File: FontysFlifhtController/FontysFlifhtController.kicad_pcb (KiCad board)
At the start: 2 copper layers, 44 x 66 mm, 25 parts, among them J1 I2C 1, J10 Motor Control 3, J11 Motor Control 4, J12 Ultrasonic Sensor, J13 Battery Power, J14 RaspberryPi, J2 I2C 2, J3 SPI 1, J4 SPI 2, J6 Camera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

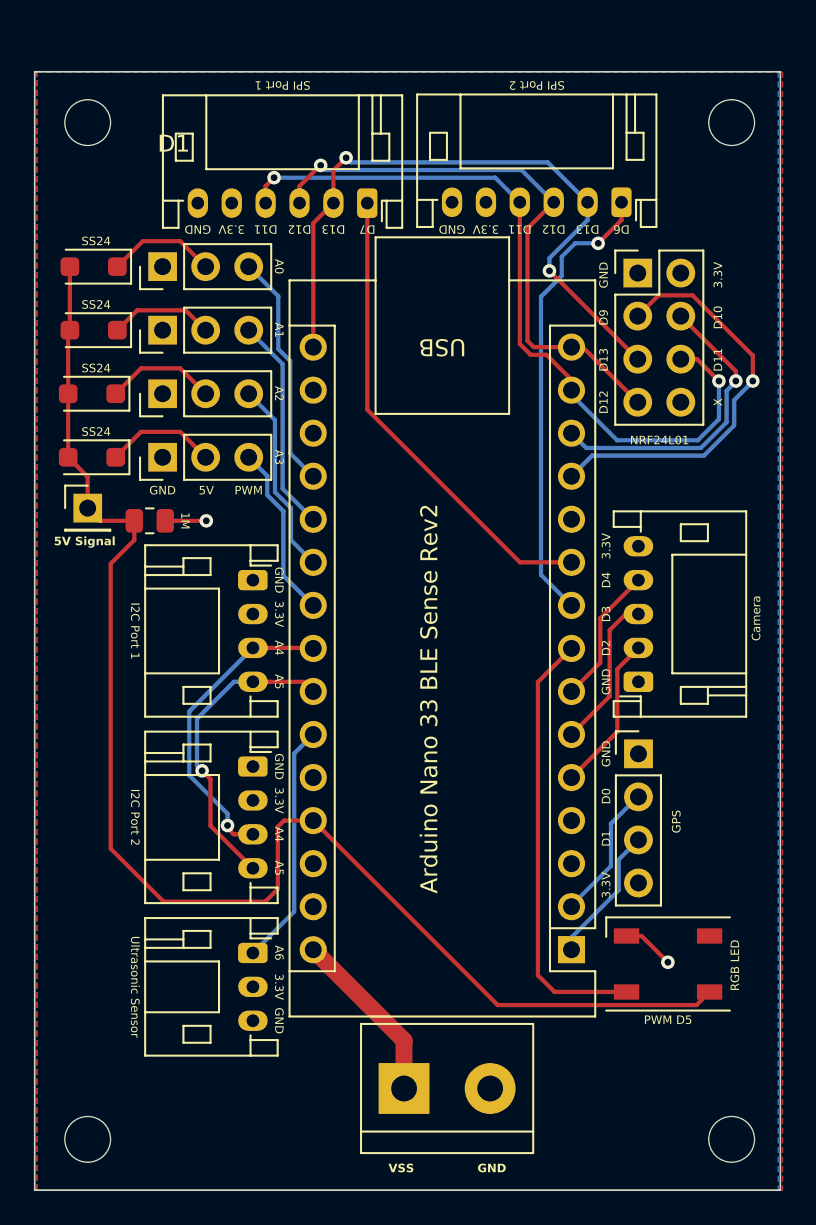
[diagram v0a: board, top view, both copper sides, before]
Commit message: Add turn on/off functionality for the motors
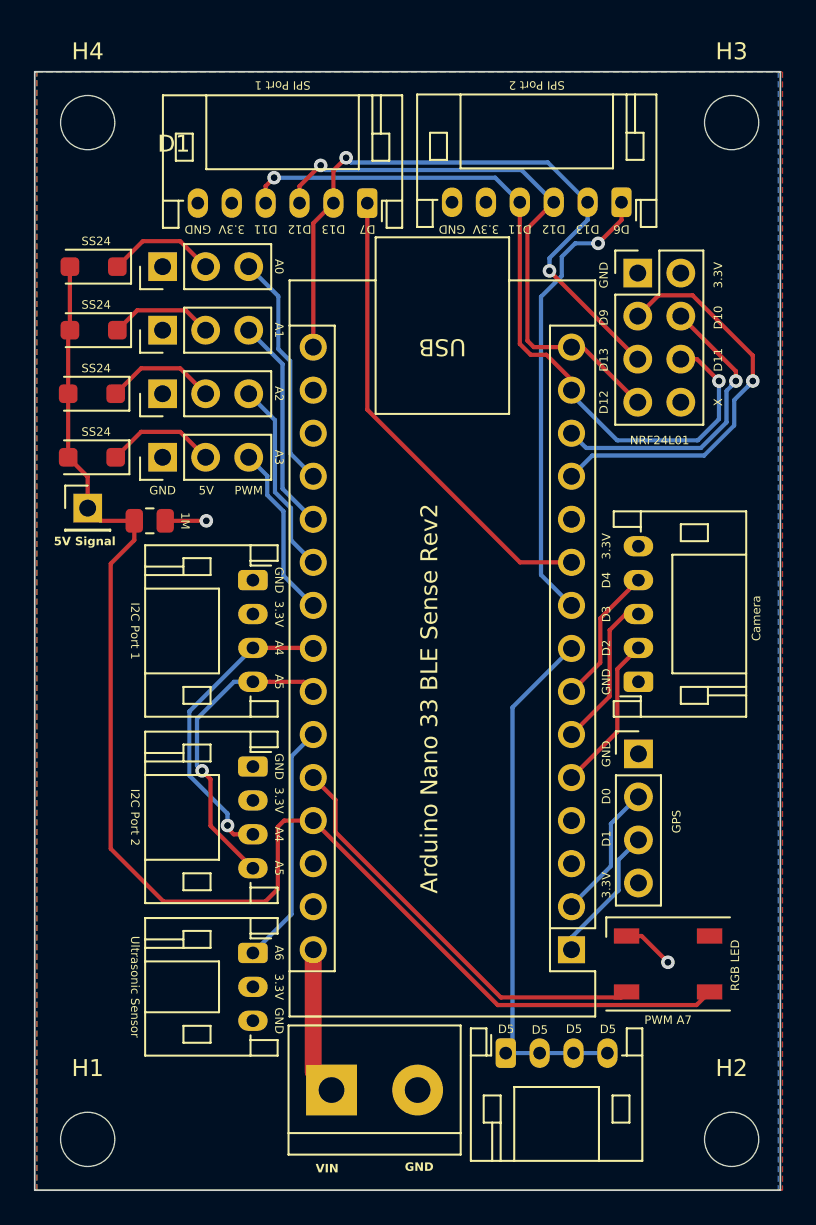
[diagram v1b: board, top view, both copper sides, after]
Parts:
- added J5: Motors On/Off, Connector_JST:JST_PH_S4B-PH-K_1x04_P2.00mm_Horizontal, F.Cu at (136.2, 127.9)
- H1, H2, H3, H4: footprint MountingHole:MountingHole_2.7mm_M2.5 -> MountingHole:MountingHole_3.2mm_M3
- moved J13 4.28 mm to (125.9, 130.1)
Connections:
- A1 pad 26: unconnected-(A1-A7-Pad26) -> /A7
- D2 pad 4: /D5 -> /A7
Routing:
- net /A7: track 0.00 -> 25.1 mm
- net /D5: track 25.7 -> 31.5 mm
- net /VIN: track 10.4 -> 8.73 mm
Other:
- board text added: "D5"
- board text added: "PWM A7"
- board text added: "VIN"
- board text removed: "PWM D5"
- board text removed: "VSS"

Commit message: Improve board
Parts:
- added J15: Motor 2 On/Off, Connector_PinHeader_2.54mm:PinHeader_1x03_P2.54mm_Vertical, F.Cu at (136.2, 128.5)
- added J16: Motor 3 On/Off, Connector_PinHeader_2.54mm:PinHeader_1x03_P2.54mm_Vertical, F.Cu at (139.8, 128.5)
- added J17: Motor 4 On/Off, Connector_PinHeader_2.54mm:PinHeader_1x03_P2.54mm_Vertical, F.Cu at (143.5, 128.5)
- H1, H2, H3, H4: footprint MountingHole:MountingHole_3.2mm_M3 -> MountingHole:MountingHole_2.7mm_M2.5
- J5: value Motors On/Off -> Motor 1 On/Off; footprint Connector_JST:JST_PH_S4B-PH-K_1x04_P2.00mm_Horizontal -> Connector_PinHeader_2.54mm:PinHeader_1x03_P2.54mm_Vertical
- moved J1 4.37 mm to (117.0, 101.0)
- moved J12 4.37 mm to (117.0, 123.0)
- moved J2 4.37 mm to (117.0, 112.0)
- moved J13 4.14 mm to (121.8, 130.0)
- moved J5 3.72 mm to (132.5, 128.5)
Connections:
- J5 pad 2: /D5 -> /3.3V
- J5 pad 3: /D5 -> GND
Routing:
- net /D5: track 31.5 -> 40.1 mm
- net /A4: track 18.4 -> 24.4 mm
- net /A5: track 18.2 -> 23.4 mm
- net /5V: track 83.7 -> 88.0 mm
- net /A6: track 14.4 -> 17.1 mm
- net /A7: track 25.1 -> 27.0 mm
- net /D4: track 8.21 -> 9.04 mm
- net /D3: track 9.19 -> 9.99 mm
- net /VIN: track 8.73 -> 9.46 mm
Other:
- outline, holes or cut-outs redrawn
- board text added: "Switch"

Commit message: final changes
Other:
- board text added: "M2.5"
- board text removed: "M3"

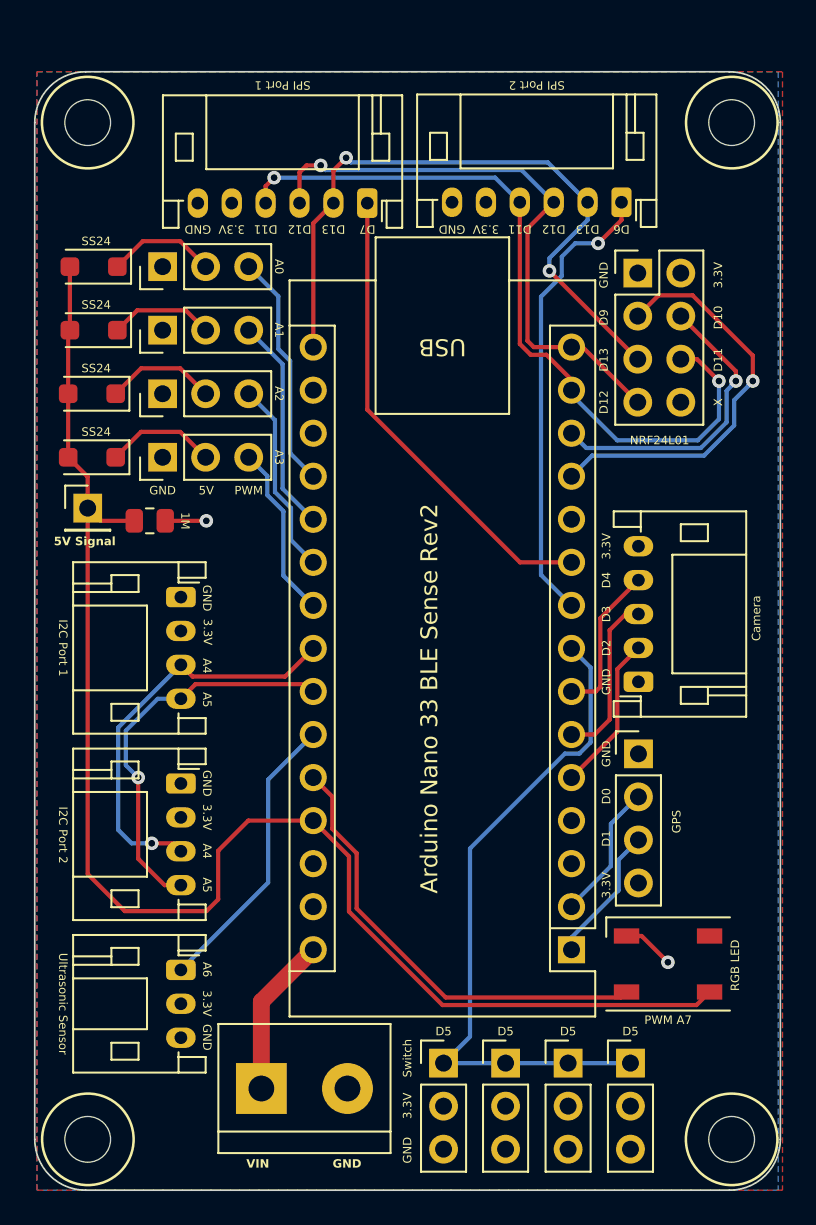
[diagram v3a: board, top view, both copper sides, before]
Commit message: edit labels
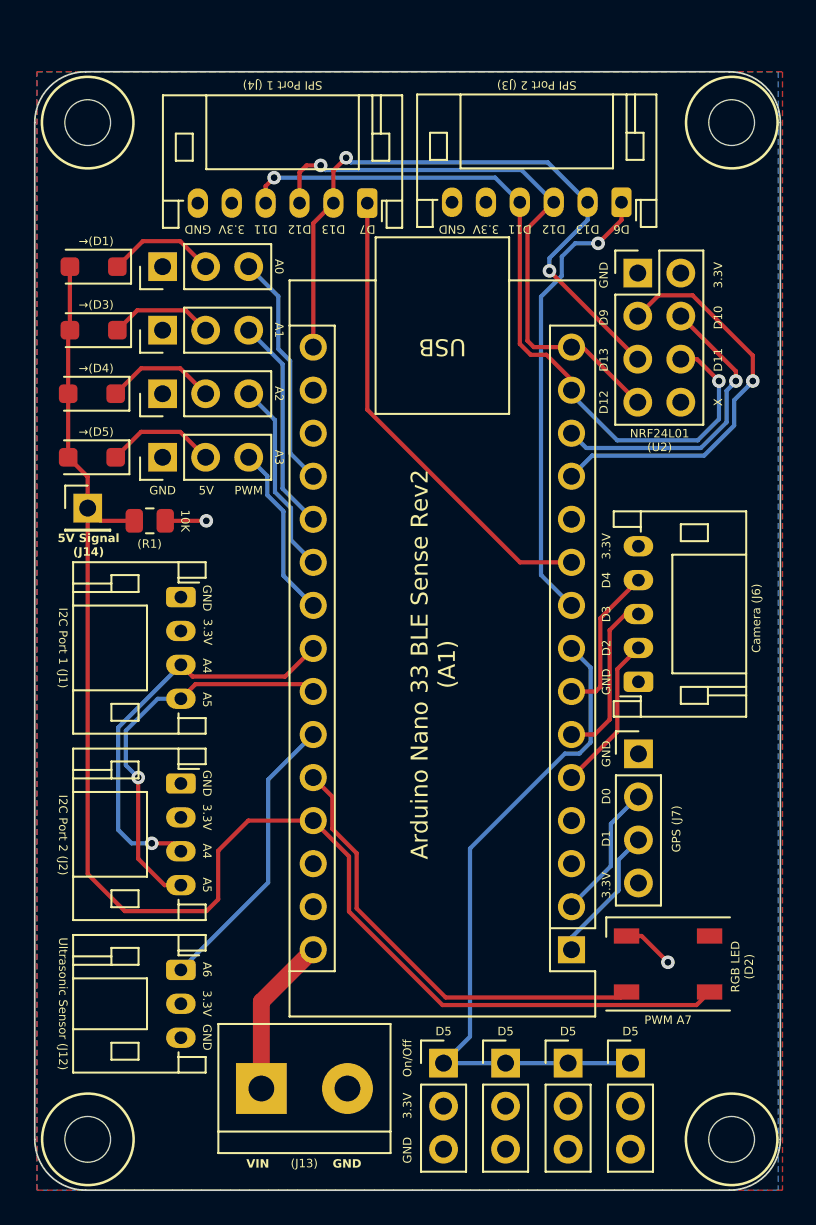
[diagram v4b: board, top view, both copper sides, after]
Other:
- board text added: "(J13)"
- board text added: "(R1)"
- board text added: "10K"
- board text added: "5V Signal (J14)"
- board text added: "Arduino Nano 33 BLE Sense Rev2 (A1)"
- board text added: "Camera (J6)"
- board text added: "GPS (J7)"
- board text added: "I2C Port 1 (J1)"
- board text added: "I2C Port 2 (J2)"
- board text added: "NRF24L01 (U2)"
- board text added: "On/Off"
- board text added: "RGB LED (D2)"
- board text added: "SPI Port 1 (J4)"
- board text added: "SPI Port 2 (J3)"
- board text added: "Ultrasonic Sensor (J12)"
- board text added: "→(D1)"
- board text added: "→(D3)"
- board text added: "→(D4)"
- board text added: "→(D5)"
- board text removed: "1M"
- board text removed: "5V Signal"
- board text removed: "Arduino Nano 33 BLE Sense Rev2"
- board text removed: "Camera"
- board text removed: "GPS"
- board text removed: "I2C Port 1"
- board text removed: "I2C Port 2"
- board text removed: "NRF24L01"
- board text removed: "RGB LED"
- board text removed: "SPI Port 1"
- board text removed: "SPI Port 2"
- board text removed: "SS24"
- board text removed: "Switch"
- board text removed: "Ultrasonic Sensor"
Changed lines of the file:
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@@
     (effects (font (size 0.5 0.5) (thickness 0.125)) (justify bottom))
   )
-  (gr_text "SS24" (at 112 80) (layer "F.SilkS")
+  (gr_text "→(D1)" (at 112 80) (layer "F.SilkS")
     (effects (font (size 0.5 0.5) (thickness 0.125)))
   )
@@
     (effects (font (size 0.5 0.5) (thickness 0.125)) (justify bottom))
   )
-  (gr_text "SPI Port 1" (at 123 70.5 180) (layer "F.SilkS")
+  (gr_text "SPI Port 1 (J4)" (at 123 70.5 180) (layer "F.SilkS")
     (effects (font (size 0.5 0.5) (thickness 0.125)) (justify bottom))
   )
@@
     (effects (font (size 0.5 0.5) (thickness 0.125)) (justify bottom))
   )
-  (gr_text "SS24" (at 112 87.5) (layer "F.SilkS")
+  (gr_text "→(D4)" (at 112 87.5) (layer "F.SilkS")
     (effects (font (size 0.5 0.5) (thickness 0.125)))
   )
@@
     (effects (font (size 0.5 0.5) (thickness 0.125)) (justify bottom))
   )
-  (gr_text "SPI Port 2" (at 138 70.5 180) (layer "F.SilkS")
+  (gr_text "SPI Port 2 (J3)" (at 138 70.5 180) (layer "F.SilkS")
     (effects (font (size 0.5 0.5) (thickness 0.125)) (justify bottom))
   )
@@
     (effects (font (size 0.5 0.5) (thickness 0.125)) (justify bottom))
   )
-  (gr_text "I2C Port 2" (at 109.75 115.04 270) (layer "F.SilkS")
+  (gr_text "I2C Port 2 (J2)" (at 109.75 115.04 270) (layer "F.SilkS")
     (effects (font (size 0.5 0.5) (thickness 0.125)) (justify bottom))
   )
@@
     (effects (font (size 0.5 0.5) (thickness 0.125)) (justify bottom))
   )
-  (gr_text "Arduino Nano 33 BLE Sense Rev2" (at 132.25 118.5 90) (layer "F.SilkS")
-    (effects (font (size 1 1) (thickness 0.15)) (justify left bottom))
+  (gr_text "Arduino Nano 33 BLE Sense Rev2\n(A1)" (at 133.29 104.97 90) (layer "F.SilkS")
+    (effects (font (size 1 1) (thickness 0.15)) (justify bottom))
   )
   (gr_text "D11" (at 149 87 90) (layer "F.SilkS")
@@
     (effects (font (size 0.5 0.5) (thickness 0.125)) (justify bottom))
   )
-  (gr_text "1M" (at 117.25 96.5 270) (layer "F.SilkS")
-    (effects (font (size 0.5 0.5) (thickness 0.125)))
-  )
-  (gr_text "Ultrasonic Sensor" (at 109.75 125 270) (layer "F.SilkS")
+  (gr_text "10K" (at 117.25 96.5 270) (layer "F.SilkS")
+    (effects (font (size 0.5 0.5) (thickness 0.125)))
+  )
+  (gr_text "Ultrasonic Sensor (J12)" (at 109.75 125 270) (layer "F.SilkS")
     (effects (font (size 0.5 0.5) (thickness 0.125)) (justify bottom))
   )
@@
     (effects (font (size 0.5 0.5) (thickness 0.125)) (justify bottom))
   )
-  (gr_text "NRF24L01" (at 145.25 91.75) (layer "F.SilkS")
+  (gr_text "NRF24L01\n(U2)" (at 145.25 91.75) (layer "F.SilkS")
     (effects (font (size 0.5 0.5) (thickness 0.125)))
   )
@@
     (effects (font (size 0.5 0.5) (thickness 0.125)) (justify bottom))
   )
-  (gr_text "I2C Port 1" (at 109.75 104 270) (layer "F.SilkS")
+  (gr_text "I2C Port 1 (J1)" (at 109.75 104 270) (layer "F.SilkS")
     (effects (font (size 0.5 0.5) (thickness 0.125)) (justify bottom))
   )
@@
     (effects (font (size 0.5 0.5) (thickness 0.125)) (justify bottom))
   )
-  (gr_text "Camera" (at 151.25 102.25 90) (layer "F.SilkS")
+  (gr_text "Camera (J6)" (at 151.25 102.25 90) (layer "F.SilkS")
     (effects (font (size 0.5 0.5) (thickness 0.125)) (justify bottom))
   )
@@
     (effects (font (size 0.5 0.5) (thickness 0.125)) (justify bottom))
   )
-  (gr_text "5V Signal" (at 109.5 98) (layer "F.SilkS")
-    (effects (font (size 0.5 0.5) (thickness 0.125) bold) (justify left bottom))
+  (gr_text "5V Signal\n(J14)" (at 111.55 98.62) (layer "F.SilkS")
+    (effects (font (size 0.5 0.5) (thickness 0.125) bold) (justify bottom))
   )
   (gr_text "GND" (at 115.92 95) (layer "F.SilkS")
@@
     (effects (font (size 0.5 0.5) (thickness 0.125)) (justify bottom))
   )
-  (gr_text "Switch" (at 130.66 128.21 90) (layer "F.SilkS")
+  (gr_text "On/Off" (at 130.66 128.21 90) (layer "F.SilkS")
+    (effects (font (size 0.5 0.5) (thickness 0.125)) (justify bottom))
+  )
+  (gr_text "(J13)" (at 124.28 134.71) (layer "F.SilkS")
     (effects (font (size 0.5 0.5) (thickness 0.125)) (justify bottom))
   )
@@
     (effects (font (size 0.5 0.5) (thickness 0.125)) (justify bottom))
   )
-  (gr_text "SS24" (at 112 83.75) (layer "F.SilkS")
+  (gr_text "→(D3)" (at 112 83.75) (layer "F.SilkS")
     (effects (font (size 0.5 0.5) (thickness 0.125)))
   )
@@
     (effects (font (size 0.5 0.5) (thickness 0.125)) (justify bottom))
   )
-  (gr_text "RGB LED" (at 150 124.25 90) (layer "F.SilkS")
-    (effects (font (size 0.5 0.5) (thickness 0.125)) (justify left bottom))
+  (gr_text "(R1)" (at 115.15 97.86) (layer "F.SilkS")
+    (effects (font (size 0.5 0.5) (thickness 0.125)))
+  )
+  (gr_text "RGB LED\n(D2)" (at 150.82 122.81 90) (layer "F.SilkS")
+    (effects (font (size 0.5 0.5) (thickness 0.125)) (justify bottom))
   )
   (gr_text "5V" (at 118.5 95) (layer "F.SilkS")
     (effects (font (size 0.5 0.5) (thickness 0.125)) (justify bottom))
   )
-  (gr_text "GPS" (at 146.25 114.25 90) (layer "F.SilkS")
+  (gr_text "GPS (J7)" (at 146.24 114.68 90) (layer "F.SilkS")
     (effects (font (size 0.5 0.5) (thickness 0.125)))
   )
@@
     (effects (font (size 0.5 0.5) (thickness 0.125)) (justify bottom))
   )
-  (gr_text "SS24" (at 112 91.25) (layer "F.SilkS")
-    (effects (font (size 0.5 0.5) (thickness 0.125)))
-  )
+  (gr_text "→(D5)" (at 112 91.25) (layer "F.SilkS")
+    (effects (font (size 0.5 0.5) (thickness 0.125)))
+  )

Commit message: add changes for feedback
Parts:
- removed J14: RaspberryPi, Connector_PinHeader_2.54mm:PinHeader_1x01_P2.54mm_Vertical
- added D6: SS24, Diode_SMD:D_SOD-123F, F.Cu at (121.7, 123.8)
- added J18: RaspberryPi, Connector_PinHeader_2.54mm:PinHeader_1x02_P2.54mm_Vertical, F.Cu at (115.9, 96.6)
- moved R1 6.32 mm to (120.7, 99.5)
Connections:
- J13 pad 1: /VIN -> Net-(D6-A)
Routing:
- net /5V: track 88.0 -> 97.7 mm
- net /VIN: track 9.46 -> 3.29 mm
- net Net-(D6-A): track 0.00 -> 5.02 mm
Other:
- board text added: "5V Signal (J18)"
- board text added: "→(D6)"
- board text removed: "5V Signal (J14)"
